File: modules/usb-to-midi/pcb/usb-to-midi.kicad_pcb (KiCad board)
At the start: 2 copper layers, 17.5 x 107.3 mm, 22 parts, among them J1 USB_B, J2 MIDI out, J3 DEBUG HEADER, U1 ATmega32U2-AU, Y1 16mhz

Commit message: usb-to-midi: fix some metadata, add schematic pdf
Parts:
- C2: value 10 -> 10u
- U1: value ATmega32U2-AU -> ATmega8U2-AU
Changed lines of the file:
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@@
-(kicad_pcb (version 20171130) (host pcbnew 5.99.0+really5.1.10+dfsg1-1+b1)
+(kicad_pcb (version 20171130) (host pcbnew 5.99.0+really5.1.12+dfsg1-1)
   (general
     (thickness 1.6)
@@
   (page A4)
   (title_block
-    (title "usb-to-midi board")
+    (title "usb-to-midi")
     (date 2021-12-13)
     (rev 1.0)
@@
       (effects (font (size 1 1) (thickness 0.15)) (justify mirror))
     )
-    (fp_text value 10 (at 1.25 -3.75 270) (layer B.Fab)
+    (fp_text value 10u (at 1.25 -3.75 270) (layer B.Fab)
       (effects (font (size 1 1) (thickness 0.15)) (justify mirror))
     )
@@
       (effects (font (size 1 1) (thickness 0.15)))
     )
-    (fp_text value ATmega32U2-AU (at 0 6.9596) (layer F.Fab)
-      (effects (font (size 1 1) (thickness 0.15)))
-    )
+    (fp_text value ATmega8U2-AU (at 0 6.9596) (layer F.Fab)
+      (effects (font (size 1 1) (thickness 0.15)))
+    )

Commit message: modules: usb-to-midi: fix references
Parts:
- D1: value LED -> LED Red
- D2: value LED -> LED Green
- J1: value USB_B -> USB Type B Vertical
- J2: value MIDI out -> Thonkiconn ST
- J3: value DEBUG HEADER -> JST XH 1x2
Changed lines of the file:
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@@
   (page A4)
   (title_block
-    (title "usb-to-midi")
+    (title usb-to-midi)
     (date 2021-12-13)
     (rev 1.0)
@@
     (46 B.CrtYd user)
     (47 F.CrtYd user)
-    (48 B.Fab user)
+    (48 B.Fab user hide)
     (49 F.Fab user hide)
   )
@@
       (effects (font (size 1 1) (thickness 0.15)) (justify mirror))
     )
-    (fp_text value "DEBUG HEADER" (at 1.25 -4.6 90) (layer B.Fab)
+    (fp_text value "JST XH 1x2" (at 1.25 -4.6 90) (layer B.Fab)
       (effects (font (size 1 1) (thickness 0.15)) (justify mirror))
     )
@@
       (effects (font (size 1 1) (thickness 0.15)))
     )
-    (fp_text value "MIDI out" (at 0 -5) (layer F.Fab)
+    (fp_text value "Thonkiconn ST" (at 0 -5) (layer F.Fab)
       (effects (font (size 1 1) (thickness 0.15)))
     )
@@
       (effects (font (size 1 1) (thickness 0.15)))
     )
-    (fp_text value USB_B (at -1.25 10.25) (layer F.Fab)
+    (fp_text value "USB Type B Vertical" (at -1.25 10.25) (layer F.Fab)
       (effects (font (size 1 1) (thickness 0.15)))
     )
@@
       (effects (font (size 1 1) (thickness 0.15)))
     )
-    (fp_text value LED (at 1.27 2.96) (layer F.Fab)
+    (fp_text value "LED Green" (at 1.27 2.96) (layer F.Fab)
       (effects (font (size 1 1) (thickness 0.15)))
     )
@@
       (effects (font (size 1 1) (thickness 0.15)))
     )
-    (fp_text value LED (at 1.27 2.96) (layer F.Fab)
-      (effects (font (size 1 1) (thickness 0.15)))
-    )
+    (fp_text value "LED Red" (at 1.27 2.96) (layer F.Fab)
+      (effects (font (size 1 1) (thickness 0.15)))
+    )

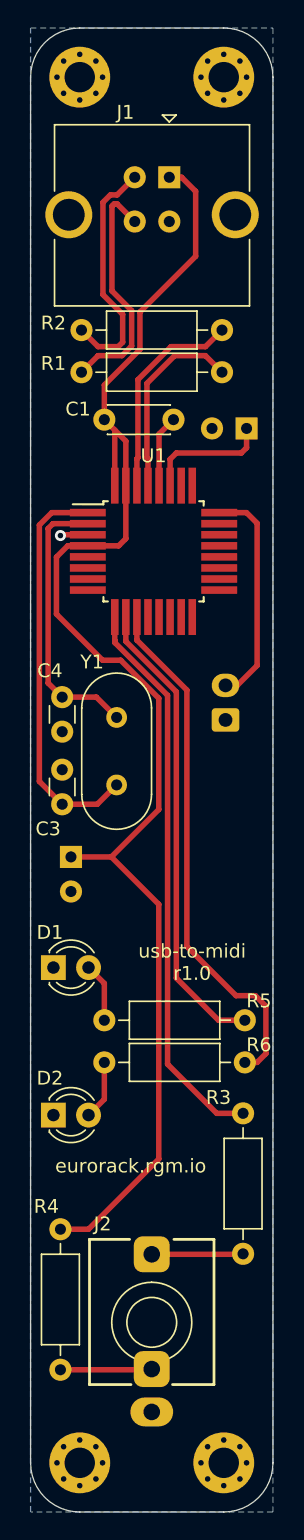
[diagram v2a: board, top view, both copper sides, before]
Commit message: modules: usb-to-midi: upgrade to kicad 6
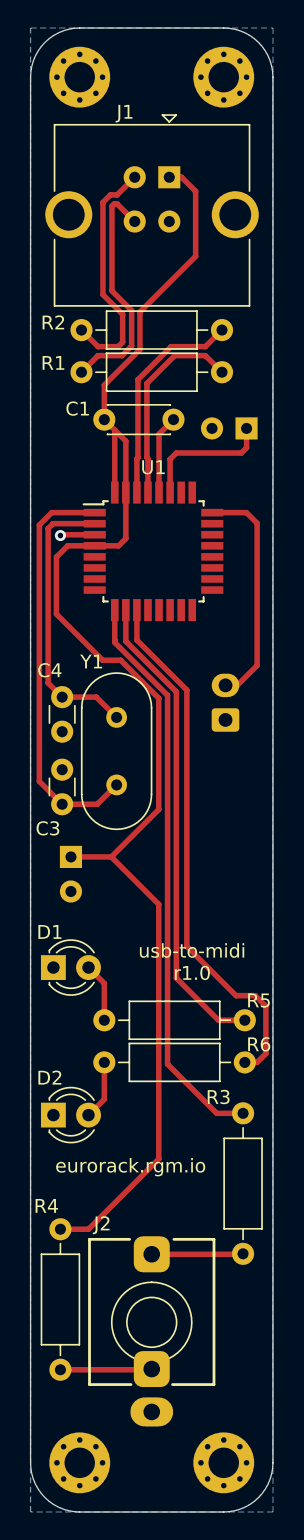
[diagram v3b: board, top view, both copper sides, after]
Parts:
- U1: footprint eurorack:TQFP-32_7x7mm_P0.8mm_LongPads -> Package_QFP:TQFP-32_7x7mm_P0.8mm
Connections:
- U1 pad 12: (no net) -> unconnected-(U1-Pad12)
- U1 pad 13: (no net) -> unconnected-(U1-Pad13)
- U1 pad 14: (no net) -> unconnected-(U1-Pad14)
- U1 pad 15: (no net) -> unconnected-(U1-Pad15)
- U1 pad 16: (no net) -> unconnected-(U1-Pad16)
- U1 pad 17: (no net) -> unconnected-(U1-Pad17)
- U1 pad 18: (no net) -> unconnected-(U1-Pad18)
- U1 pad 19: (no net) -> unconnected-(U1-Pad19)
- U1 pad 20: (no net) -> unconnected-(U1-Pad20)
- U1 pad 21: (no net) -> unconnected-(U1-Pad21)
- U1 pad 22: (no net) -> unconnected-(U1-Pad22)
- U1 pad 23: (no net) -> unconnected-(U1-Pad23)
- U1 pad 25: (no net) -> unconnected-(U1-Pad25)
- U1 pad 26: (no net) -> unconnected-(U1-Pad26)
- U1 pad 5: (no net) -> unconnected-(U1-Pad5)
- U1 pad 6: (no net) -> unconnected-(U1-Pad6)
- U1 pad 7: (no net) -> unconnected-(U1-Pad7)
- U1 pad 8: (no net) -> unconnected-(U1-Pad8)
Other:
- net class Default removed
